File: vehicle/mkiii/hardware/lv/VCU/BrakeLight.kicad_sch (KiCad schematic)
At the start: 21 parts, among them Q3 SSM3K333R,LF, U7 MCP6001T-I/LT, U8 MCP6001T-I/LT, U9 U_GATE_SN74LVC1G32DBVR

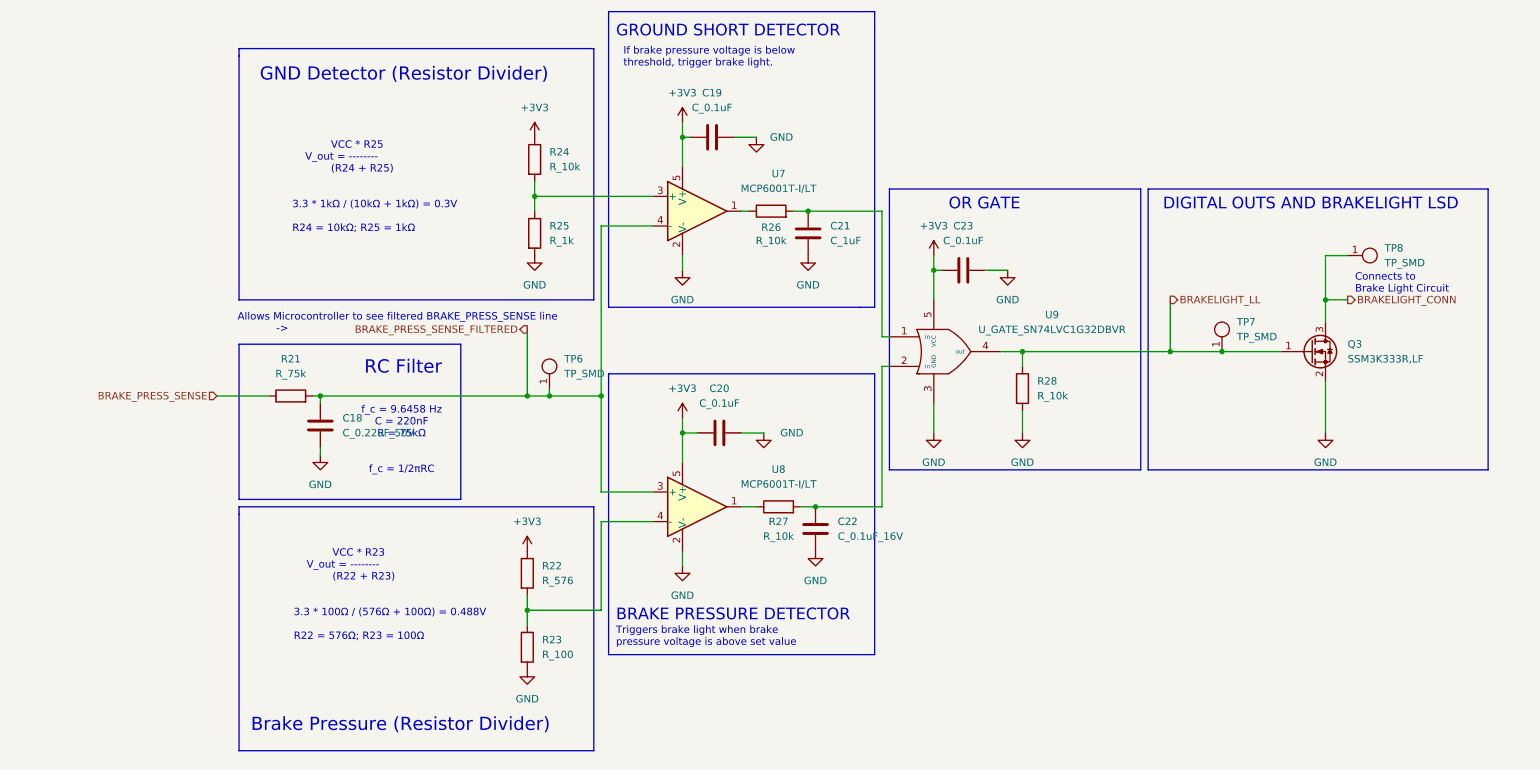
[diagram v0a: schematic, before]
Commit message: Resolved some "footprint not exist" issues
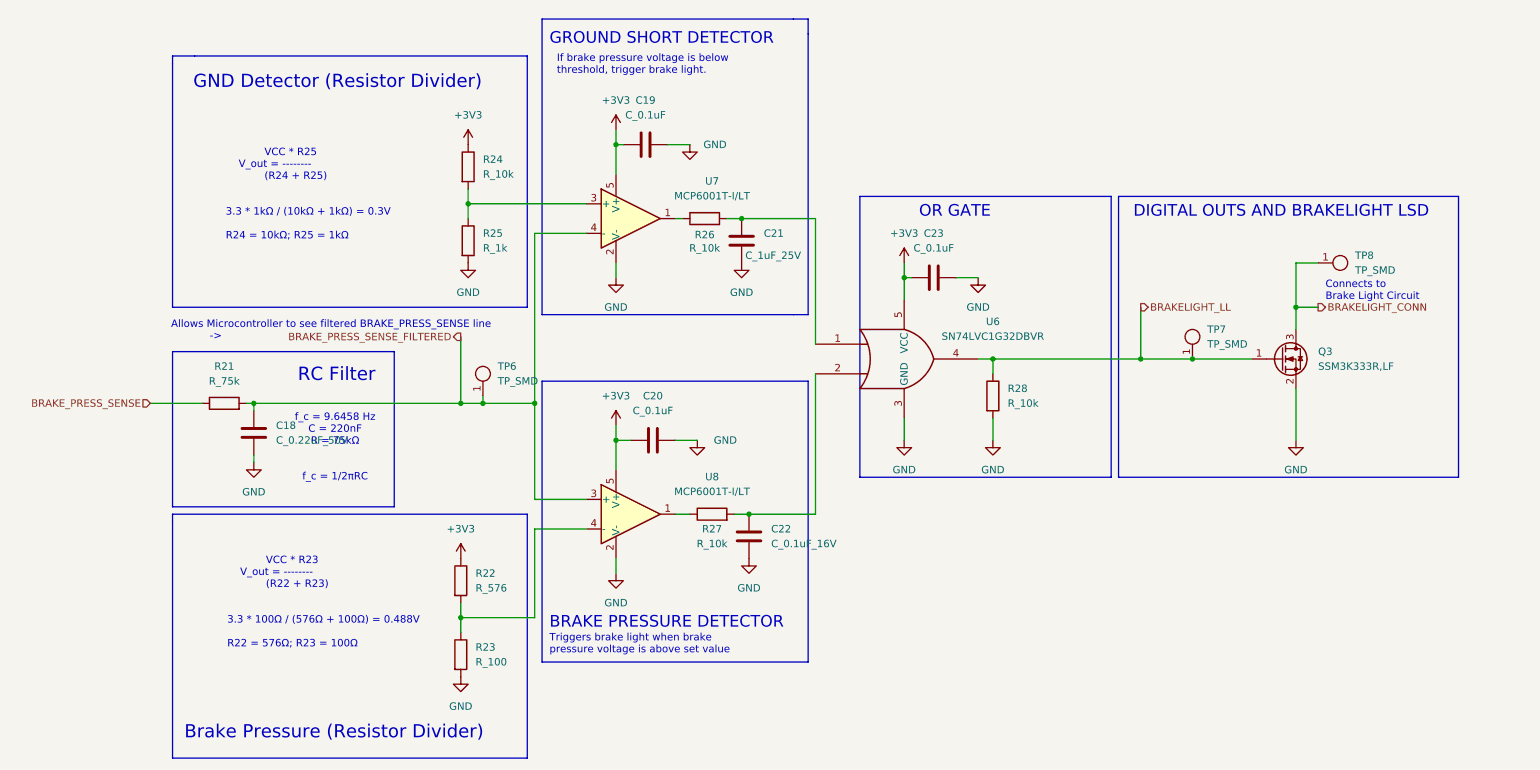
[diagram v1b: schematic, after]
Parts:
- removed U9: U_GATE_SN74LVC1G32DBVR, OEM:SOT-23-5_OEM, symbol OEM:U_GATE_SN74LVC1G32DBVR
- added U6: SN74LVC1G32DBVR, OEM:SOT-23-5, symbol OEM:U_OR-Gate_SN74LVC1G32DBVR_SOT23-5
- C21: value C_1uF -> C_1uF_25V; footprint OEM:C_0603 -> OEM:C_0603_1608Metric; symbol OEM:C_1uF -> OEM:C_1uF_25V_0603
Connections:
- net +3V3: now also U6.5 (VCC)
- net BRAKELIGHT_LL: now also U6.4
- net GND: now also U6.3 (GND)
- net at C22.1, R27.2: now also U6.2
- net at C21.1, R26.2: now also U6.1
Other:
- moved on the sheet: C18, C19, C20, C21, C22, C23, Q3, R21, R22, R23, R24, R25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

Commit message: Layout completed, review required
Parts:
- renumbered C18 to C22, C19 to C23, C20 to C24, C21 to C25, C22 to C26, C23 to C27, R21 to R29, R22 to R30, R23 to R31, R24 to R32, R25 to R33, R26 to R34, R27 to R35, R28 to R36, TP6 to TP7, TP7 to TP8, TP8 to TP9, U6 to U10, U7 to U8, U8 to U9
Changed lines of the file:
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@@
 		(color 0 0 0 0)
 	)
+	(bus_entry
+		(at 76.2 109.22)
+		(size 2.54 2.54)
+		(stroke
+			(width 0)
+			(type default)
+		)
+	)
 	(wire
 		(pts
@@
 		(dnp no)
 		(fields_autoplaced yes)
-		(property "Reference" "C23"
+		(property "Reference" "C27"
 			(at 176.53 76.2 90)
 			(effects
@@
 			(project "VCU"
 				(path "/ec5dd9e3-3092-4af4-bee1-94131d9ab7f8/c320cd2f-9217-4ab2-b275-be2d18e0c35c"
-					(reference "C23")
+					(reference "C27")
 					(unit 1)
 				)
@@
 		(dnp no)
 		(fields_autoplaced yes)
-		(property "Reference" "R25"
+		(property "Reference" "R33"
 			(at 99.06 76.1999 0)
 			(effects
@@
 			(project ""
 				(path "/ec5dd9e3-3092-4af4-bee1-94131d9ab7f8/c320cd2f-9217-4ab2-b275-be2d18e0c35c"
-					(reference "R25")
+					(reference "R33")
 					(unit 1)
 				)
@@
 		(on_board yes)
 		(dnp no)
-		(property "Reference" "R27"
+		(property "Reference" "R35"
 			(at 138.43 127 90)
 			(effects
@@
 			(project "VCU"
 				(path "/ec5dd9e3-3092-4af4-bee1-94131d9ab7f8/c320cd2f-9217-4ab2-b275-be2d18e0c35c"
-					(reference "R27")
+					(reference "R35")
 					(unit 1)
 				)
@@
 		(on_board yes)
 		(dnp no)
-		(property "Reference" "C21"
+		(property "Reference" "C25"
 			(at 147.32 76.1999 0)
 			(effects
@@
 			(project "VCU"
 				(path "/ec5dd9e3-3092-4af4-bee1-94131d9ab7f8/c320cd2f-9217-4ab2-b275-be2d18e0c35c"
-					(reference "C21")
+					(reference "C25")
 					(unit 1)
 				)
@@
 		(dnp no)
 		(fields_autoplaced yes)
-		(property "Reference" "TP7"
+		(property "Reference" "TP8"
 			(at 223.52 92.7099 0)
 			(effects
@@
 			(project ""
 				(path "/ec5dd9e3-3092-4af4-bee1-94131d9ab7f8/c320cd2f-9217-4ab2-b275-be2d18e0c35c"
-					(reference "TP7")
+					(reference "TP8")
 					(unit 1)
 				)
@@
 		(dnp no)
 		(fields_autoplaced yes)
-		(property "Reference" "C22"
+		(property "Reference" "C26"
 			(at 148.59 126.9999 0)
 			(effects
@@
 			(project ""
 				(path "/ec5dd9e3-3092-4af4-bee1-94131d9ab7f8/c320cd2f-9217-4ab2-b275-be2d18e0c35c"
-					(reference "C22")
+					(reference "C26")
 					(unit 1)
 				)
@@
 		(on_board yes)
 		(dnp no)
-		(property "Reference" "R26"
+		(property "Reference" "R34"
 			(at 137.16 76.454 90)
 			(effects
@@
 			(project "VCU"
 				(path "/ec5dd9e3-3092-4af4-bee1-94131d9ab7f8/c320cd2f-9217-4ab2-b275-be2d18e0c35c"
-					(reference "R26")
+					(reference "R34")
 					(unit 1)
 				)
@@
 		(dnp no)
 		(fields_autoplaced yes)
-		(property "Reference" "R21"
+		(property "Reference" "R29"
 			(at 54.61 99.06 90)
 			(effects
@@
 			(project ""
 				(path "/ec5dd9e3-3092-4af4-bee1-94131d9ab7f8/c320cd2f-9217-4ab2-b275-be2d18e0c35c"
-					(reference "R21")
+					(reference "R29")
 					(unit 1)
 				)
@@
 		(dnp no)
 		(fields_autoplaced yes)
-		(property "Reference" "TP6"
+		(property "Reference" "TP7"
 			(at 101.6 99.0599 0)
 			(effects
@@
 			(project ""
 				(path "/ec5dd9e3-3092-4af4-bee1-94131d9ab7f8/c320cd2f-9217-4ab2-b275-be2d18e0c35c"
-					(reference "TP6")
+					(reference "TP7")
 					(unit 1)
 				)
@@
 		(dnp no)
 		(fields_autoplaced yes)
-		(property "Reference" "U7"
+		(property "Reference" "U8"
 			(at 138.43 67.2398 0)
 			(effects
@@
 			(project "VCU"
 				(path "/ec5dd9e3-3092-4af4-bee1-94131d9ab7f8/c320cd2f-9217-4ab2-b275-be2d18e0c35c"
-					(reference "U7")
+					(reference "U8")
 					(unit 1)
 				)
@@
 		(dnp no)
 		(fields_autoplaced yes)
-		(property "Reference" "TP8"
+		(property "Reference" "TP9"
 			(at 248.92 80.0099 90)
 			(effects
@@
 			(project "VCU"
 				(path "/ec5dd9e3-3092-4af4-bee1-94131d9ab7f8/c320cd2f-9217-4ab2-b275-be2d18e0c35c"
-					(reference "TP8")
+					(reference "TP9")
 					(unit 1)
 				)
@@
 		(dnp no)
 		(fields_autoplaced yes)
-		(property "Reference" "U8"
+		(property "Reference" "U9"
 			(at 138.43 118.0398 0)
 			(effects
@@
 			(project "VCU"
 				(path "/ec5dd9e3-3092-4af4-bee1-94131d9ab7f8/c320cd2f-9217-4ab2-b275-be2d18e0c35c"
-					(reference "U8")
+					(reference "U9")
 					(unit 1)
 				)
@@
 		(dnp no)
 		(fields_autoplaced yes)
-		(property "Reference" "C20"
+		(property "Reference" "C24"
 			(at 128.27 104.14 90)
 			(effects
@@
 			(project "VCU"
 				(path "/ec5dd9e3-3092-4af4-bee1-94131d9ab7f8/c320cd2f-9217-4ab2-b275-be2d18e0c35c"
-					(reference "C20")
+					(reference "C24")
 					(unit 1)
 				)
@@
 		(dnp no)
 		(fields_autoplaced yes)
-		(property "Reference" "C19"
+		(property "Reference" "C23"
 			(at 127 53.34 90)
 			(effects
@@
 			(project "VCU"
 				(path "/ec5dd9e3-3092-4af4-bee1-94131d9ab7f8/c320cd2f-9217-4ab2-b275-be2d18e0c35c"
-					(reference "C19")
+					(reference "C23")
 					(unit 1)
 				)
@@
 		(dnp no)
 		(fields_autoplaced yes)
-		(property "Reference" "C18"
+		(property "Reference" "C22"
 			(at 63.5 109.2199 0)
 			(effects
@@
 			(project ""
 				(path "/ec5dd9e3-3092-4af4-bee1-94131d9ab7f8/c320cd2f-9217-4ab2-b275-be2d18e0c35c"
-					(reference "C18")
+					(reference "C22")
 					(unit 1)
 				)
@@
 		(dnp no)
 		(fields_autoplaced yes)
-		(property "Reference" "U6"
+		(property "Reference" "U10"
 			(at 186.69 91.3698 0)
 			(effects
@@
 			(project ""
 				(path "/ec5dd9e3-3092-4af4-bee1-94131d9ab7f8/c320cd2f-9217-4ab2-b275-be2d18e0c35c"
-					(reference "U6")
+					(reference "U10")
 					(unit 1)
 				)
@@
 		(dnp no)
 		(fields_autoplaced yes)
-		(property "Reference" "R24"
+		(property "Reference" "R32"
 			(at 99.06 63.4999 0)
 			(effects
@@
 			(project "VCU"
 				(path "/ec5dd9e3-3092-4af4-bee1-94131d9ab7f8/c320cd2f-9217-4ab2-b275-be2d18e0c35c"
-					(reference "R24")
+					(reference "R32")
 					(unit 1)
 				)
@@
 		(dnp no)
 		(fields_autoplaced yes)
-		(property "Reference" "R22"
+		(property "Reference" "R30"
 			(at 97.79 134.6199 0)
 			(effects
@@
 			(project ""
 				(path "/ec5dd9e3-3092-4af4-bee1-94131d9ab7f8/c320cd2f-9217-4ab2-b275-be2d18e0c35c"
-					(reference "R22")
+					(reference "R30")
 					(unit 1)
 				)
@@
 		(dnp no)
 		(fields_autoplaced yes)
-		(property "Reference" "R23"
+		(property "Reference" "R31"
 			(at 97.79 147.3199 0)
 			(effects
@@
 			(project ""
 				(path "/ec5dd9e3-3092-4af4-bee1-94131d9ab7f8/c320cd2f-9217-4ab2-b275-be2d18e0c35c"
-					(reference "R23")
+					(reference "R31")
 					(unit 1)
 				)
@@
 		(dnp no)
 		(fields_autoplaced yes)
-		(property "Reference" "R28"
+		(property "Reference" "R36"
 			(at 189.23 102.8699 0)
 			(effects
@@
 			(project "VCU"
 				(path "/ec5dd9e3-3092-4af4-bee1-94131d9ab7f8/c320cd2f-9217-4ab2-b275-be2d18e0c35c"
-					(reference "R28")
+					(reference "R36")
 					(unit 1)
 				)

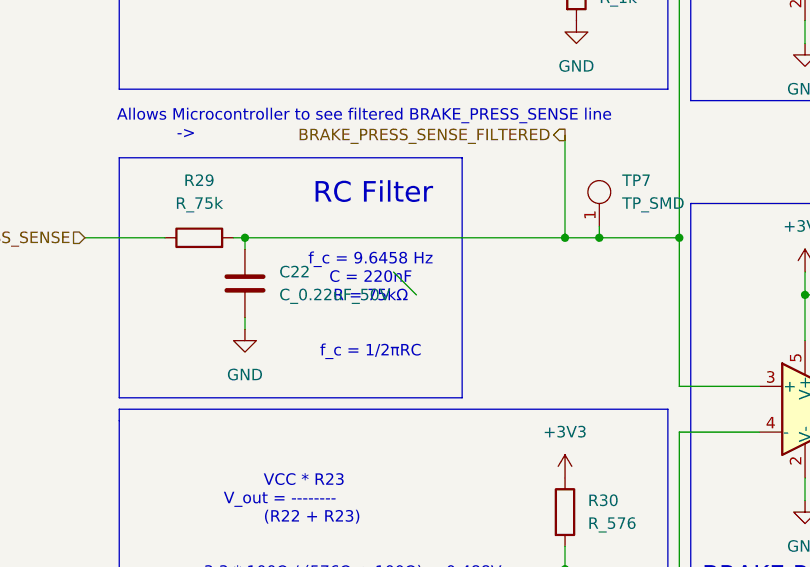
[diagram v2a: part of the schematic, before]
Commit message: Minor ERC Fixes in Schematics; Minor Silkscreen Changes; Addedc Subteam Layout; Added Production Files.
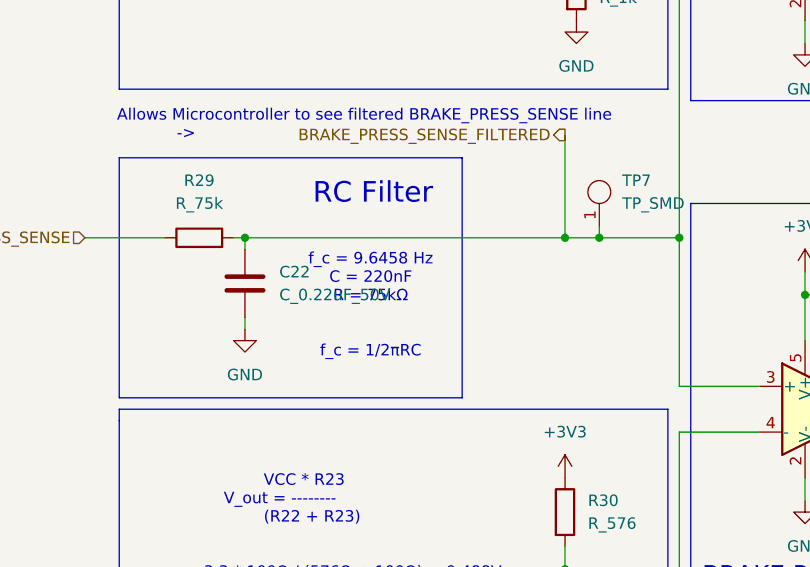
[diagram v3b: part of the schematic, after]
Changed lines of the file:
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@@
 		(color 0 0 0 0)
 	)
-	(bus_entry
-		(at 76.2 109.22)
-		(size 2.54 2.54)
-		(stroke
-			(width 0)
-			(type default)
-		)
-	)
 	(wire
 		(pts
@@
 		(on_board yes)
 		(dnp no)
-		(property "Reference" "#PWR?"
+		(property "Reference" "#PWR0181"
 			(at 134.62 67.31 0)
 			(effects
@@
 			(project "VCU"
 				(path "/ec5dd9e3-3092-4af4-bee1-94131d9ab7f8/c320cd2f-9217-4ab2-b275-be2d18e0c35c"
-					(reference "#PWR?")
+					(reference "#PWR0181")
 					(unit 1)
 				)
@@
 		(dnp no)
 		(fields_autoplaced yes)
-		(property "Reference" "#PWR?"
+		(property "Reference" "#PWR0184"
 			(at 121.92 90.17 0)
 			(effects
@@
 			(project "VCU"
 				(path "/ec5dd9e3-3092-4af4-bee1-94131d9ab7f8/c320cd2f-9217-4ab2-b275-be2d18e0c35c"
-					(reference "#PWR?")
+					(reference "#PWR0184")
 					(unit 1)
 				)
@@
 		(dnp no)
 		(fields_autoplaced yes)
-		(property "Reference" "#PWR?"
+		(property "Reference" "#PWR0183"
 			(at 143.51 87.63 0)
 			(effects
@@
 			(project "VCU"
 				(path "/ec5dd9e3-3092-4af4-bee1-94131d9ab7f8/c320cd2f-9217-4ab2-b275-be2d18e0c35c"
-					(reference "#PWR?")
+					(reference "#PWR0183")
 					(unit 1)
 				)
@@
 		(dnp no)
 		(fields_autoplaced yes)
-		(property "Reference" "#PWR?"
+		(property "Reference" "#PWR0177"
 			(at 59.69 121.92 0)
 			(effects
@@
 			(project "VCU"
 				(path "/ec5dd9e3-3092-4af4-bee1-94131d9ab7f8/c320cd2f-9217-4ab2-b275-be2d18e0c35c"
-					(reference "#PWR?")
+					(reference "#PWR0177")
 					(unit 1)
 				)
@@
 		(on_board yes)
 		(dnp no)
-		(property "Reference" "#PWR?"
+		(property "Reference" "#PWR0191"
 			(at 135.89 118.11 0)
 			(effects
@@
 			(project "VCU"
 				(path "/ec5dd9e3-3092-4af4-bee1-94131d9ab7f8/c320cd2f-9217-4ab2-b275-be2d18e0c35c"
-					(reference "#PWR?")
+					(reference "#PWR0191")
 					(unit 1)
 				)
@@
 		(dnp no)
 		(fields_autoplaced yes)
-		(property "Reference" "#PWR?"
+		(property "Reference" "#PWR0192"
 			(at 144.78 138.43 0)
 			(effects
@@
 			(project "VCU"
 				(path "/ec5dd9e3-3092-4af4-bee1-94131d9ab7f8/c320cd2f-9217-4ab2-b275-be2d18e0c35c"
-					(reference "#PWR?")
+					(reference "#PWR0192")
 					(unit 1)
 				)
@@
 		(dnp no)
 		(fields_autoplaced yes)
-		(property "Reference" "#PWR?"
+		(property "Reference" "#PWR0179"
 			(at 96.52 87.63 0)
 			(effects
@@
 			(project "VCU"
 				(path "/ec5dd9e3-3092-4af4-bee1-94131d9ab7f8/c320cd2f-9217-4ab2-b275-be2d18e0c35c"
-					(reference "#PWR?")
+					(reference "#PWR0179")
 					(unit 1)
 				)
@@
 		(dnp no)
 		(fields_autoplaced yes)
-		(property "Reference" "#PWR?"
+		(property "Reference" "#PWR0178"
 			(at 96.52 64.77 0)
 			(effects
@@
 			(project ""
 				(path "/ec5dd9e3-3092-4af4-bee1-94131d9ab7f8/c320cd2f-9217-4ab2-b275-be2d18e0c35c"
-					(reference "#PWR?")
+					(reference "#PWR0178")
 					(unit 1)
 				)
@@
 		(dnp no)
 		(fields_autoplaced yes)
-		(property "Reference" "#PWR?"
+		(property "Reference" "#PWR0189"
 			(at 121.92 140.97 0)
 			(effects
@@
 			(project "VCU"
 				(path "/ec5dd9e3-3092-4af4-bee1-94131d9ab7f8/c320cd2f-9217-4ab2-b275-be2d18e0c35c"
-					(reference "#PWR?")
+					(reference "#PWR0189")
 					(unit 1)
 				)
@@
 		(dnp no)
 		(fields_autoplaced yes)
-		(property "Reference" "#PWR?"
+		(property "Reference" "#PWR0194"
 			(at 95.25 135.89 0)
 			(effects
@@
 			(project ""
 				(path "/ec5dd9e3-3092-4af4-bee1-94131d9ab7f8/c320cd2f-9217-4ab2-b275-be2d18e0c35c"
-					(reference "#PWR?")
+					(reference "#PWR0194")
 					(unit 1)
 				)
@@
 		(dnp no)
 		(fields_autoplaced yes)
-		(property "Reference" "#PWR?"
+		(property "Reference" "#PWR0190"
 			(at 121.92 113.03 0)
 			(effects
@@
 			(project ""
 				(path "/ec5dd9e3-3092-4af4-bee1-94131d9ab7f8/c320cd2f-9217-4ab2-b275-be2d18e0c35c"
-					(reference "#PWR?")
+					(reference "#PWR0190")
 					(unit 1)
 				)
@@
 		(dnp no)
 		(fields_autoplaced yes)
-		(property "Reference" "#PWR?"
+		(property "Reference" "#PWR0188"
 			(at 171.45 85.09 0)
 			(effects
@@
 			(project ""
 				(path "/ec5dd9e3-3092-4af4-bee1-94131d9ab7f8/c320cd2f-9217-4ab2-b275-be2d18e0c35c"
-					(reference "#PWR?")
+					(reference "#PWR0188")
 					(unit 1)
 				)
@@
 		(dnp no)
 		(fields_autoplaced yes)
-		(property "Reference" "#PWR?"
+		(property "Reference" "#PWR0186"
 			(at 171.45 118.11 0)
 			(effects
@@
 			(project "VCU"
 				(path "/ec5dd9e3-3092-4af4-bee1-94131d9ab7f8/c320cd2f-9217-4ab2-b275-be2d18e0c35c"
-					(reference "#PWR?")
+					(reference "#PWR0186")
 					(unit 1)
 				)
@@
 		(dnp no)
 		(fields_autoplaced yes)
-		(property "Reference" "#PWR?"
+		(property "Reference" "#PWR0193"
 			(at 95.25 158.75 0)
 			(effects
@@
 			(project "VCU"
 				(path "/ec5dd9e3-3092-4af4-bee1-94131d9ab7f8/c320cd2f-9217-4ab2-b275-be2d18e0c35c"
-					(reference "#PWR?")
+					(reference "#PWR0193")
 					(unit 1)
 				)
@@
 		(dnp no)
 		(fields_autoplaced yes)
-		(property "Reference" "#PWR?"
+		(property "Reference" "#PWR0180"
 			(at 184.15 90.17 0)
 			(effects
@@
 			(project "VCU"
 				(path "/ec5dd9e3-3092-4af4-bee1-94131d9ab7f8/c320cd2f-9217-4ab2-b275-be2d18e0c35c"
-					(reference "#PWR?")
+					(reference "#PWR0180")
 					(unit 1)
 				)
@@
 		(dnp no)
 		(fields_autoplaced yes)
-		(property "Reference" "#PWR?"
+		(property "Reference" "#PWR0187"
 			(at 186.69 118.11 0)
 			(effects
@@
 			(project "VCU"
 				(path "/ec5dd9e3-3092-4af4-bee1-94131d9ab7f8/c320cd2f-9217-4ab2-b275-be2d18e0c35c"
-					(reference "#PWR?")
+					(reference "#PWR0187")
 					(unit 1)
 				)
@@
 		(dnp no)
 		(fields_autoplaced yes)
-		(property "Reference" "#PWR?"
+		(property "Reference" "#PWR0182"
 			(at 121.92 62.23 0)
 			(effects
@@
 			(project ""
 				(path "/ec5dd9e3-3092-4af4-bee1-94131d9ab7f8/c320cd2f-9217-4ab2-b275-be2d18e0c35c"
-					(reference "#PWR?")
+					(reference "#PWR0182")
 					(unit 1)
 				)
@@
 		(dnp no)
 		(fields_autoplaced yes)
-		(property "Reference" "#PWR?"
+		(property "Reference" "#PWR0185"
 			(at 238.76 118.11 0)
 			(effects
@@
 			(project "VCU"
 				(path "/ec5dd9e3-3092-4af4-bee1-94131d9ab7f8/c320cd2f-9217-4ab2-b275-be2d18e0c35c"
-					(reference "#PWR?")
+					(reference "#PWR0185")
 					(unit 1)
 				)
